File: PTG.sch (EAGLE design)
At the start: 96 parts, among them IC1 TPS62120, IC2 PIC32MK1024MCF064-I_PT, IC3 PCM1748, IC4 TPS561208, IC6 LT1762, IC7 LT1762, J1 STX31005NB, J2 RCJ-01X, J3 22-27-2021-02, SW1 ROCKER_SWITCH, SW2 ENCODER, SW3 MHPS2273N, SW4 MHPS2273N, SW5 MHPS2273N, SW6 MHPS2273N, X1 22-23-2041, Y1 EXTERNALCRYSTAL

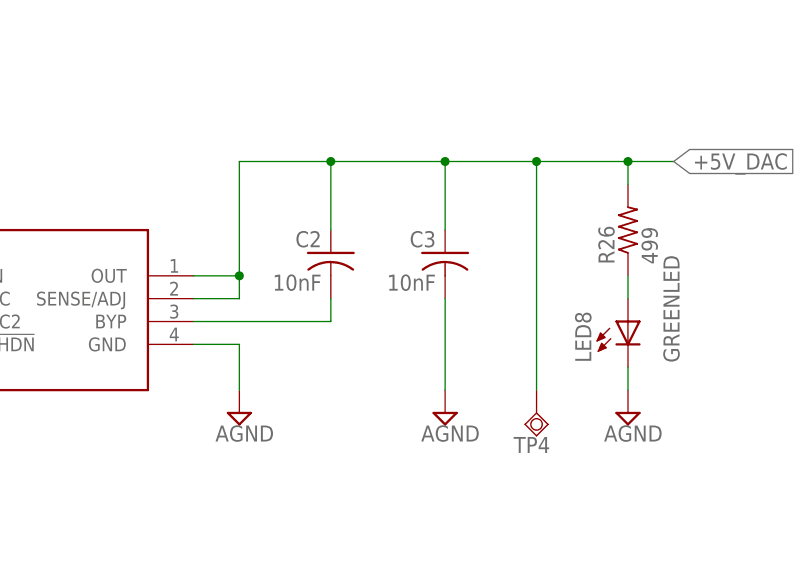
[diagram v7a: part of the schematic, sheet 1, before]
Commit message: fixed 10uF cap on IC6
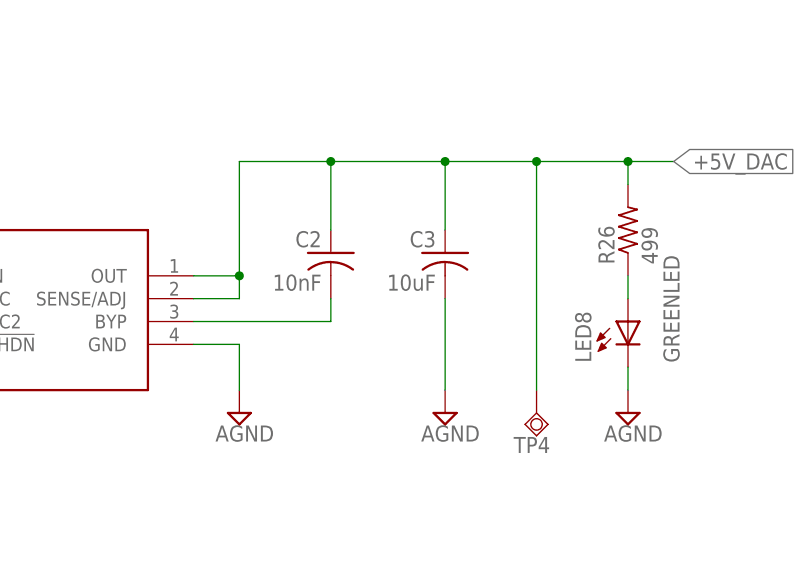
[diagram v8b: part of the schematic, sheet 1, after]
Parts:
- C3: value 10nF -> 10uF; device rcl:C-USC0603K -> rcl:C-USC0805K
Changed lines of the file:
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@@
 <grid distance="0.1" unitdist="inch" unit="inch" style="lines" multiple="1" display="no" altdistance="0.01" altunitdist="inch" altunit="inch"/>
 <layers>
-<layer number="1" name="Top" color="4" fill="1" visible="no" active="no"/>
-<layer number="2" name="Route2" color="3" fill="10" visible="no" active="no"/>
-<layer number="3" name="Route3" color="4" fill="3" visible="no" active="no"/>
-<layer number="4" name="Route4" color="1" fill="4" visible="no" active="no"/>
-<layer number="5" name="Route5" color="4" fill="4" visible="no" active="no"/>
-<layer number="6" name="Route6" color="1" fill="8" visible="no" active="no"/>
-<layer number="7" name="Route7" color="4" fill="8" visible="no" active="no"/>
-<layer number="8" name="Route8" color="1" fill="2" visible="no" active="no"/>
-<layer number="9" name="Route9" color="4" fill="2" visible="no" active="no"/>
-<layer number="10" name="Route10" color="1" fill="7" visible="no" active="no"/>
-<layer number="11" name="Route11" color="4" fill="7" visible="no" active="no"/>
-<layer number="12" name="Route12" color="1" fill="5" visible="no" active="no"/>
-<layer number="13" name="Route13" color="4" fill="5" visible="no" active="no"/>
-<layer number="14" name="Route14" color="1" fill="6" visible="no" active="no"/>
-<layer number="15" name="Route15" color="5" fill="4" visible="no" active="no"/>
-<layer number="16" name="Bottom" color="1" fill="1" visible="no" active="no"/>
-<layer number="17" name="Pads" color="2" fill="1" visible="no" active="no"/>
-<layer number="18" name="Vias" color="2" fill="1" visible="no" active="no"/>
-<layer number="19" name="Unrouted" color="60" fill="1" visible="no" active="no"/>
-<layer number="20" name="Dimension" color="15" fill="1" visible="no" active="no"/>
-<layer number="21" name="tPlace" color="7" fill="1" visible="no" active="no"/>
-<layer number="22" name="bPlace" color="7" fill="1" visible="no" active="no"/>
-<layer number="23" name="tOrigins" color="15" fill="1" visible="no" active="no"/>
-<layer number="24" name="bOrigins" color="15" fill="1" visible="no" active="no"/>
-<layer number="25" name="tNames" color="7" fill="1" visible="no" active="no"/>
-<layer number="26" name="bNames" color="7" fill="1" visible="no" active="no"/>
-<layer number="27" name="tValues" color="7" fill="1" visible="no" active="no"/>
-<layer number="28" name="bValues" color="7" fill="1" visible="no" active="no"/>
+<layer number="1" name="Top" color="4" fill="1" visible="yes" active="no"/>
+<layer number="2" name="Route2" color="3" fill="10" visible="yes" active="no"/>
+<layer number="3" name="Route3" color="4" fill="3" visible="yes" active="no"/>
+<layer number="4" name="Route4" color="1" fill="4" visible="yes" active="no"/>
+<layer number="5" name="Route5" color="4" fill="4" visible="yes" active="no"/>
+<layer number="6" name="Route6" color="1" fill="8" visible="yes" active="no"/>
+<layer number="7" name="Route7" color="4" fill="8" visible="yes" active="no"/>
+<layer number="8" name="Route8" color="1" fill="2" visible="yes" active="no"/>
+<layer number="9" name="Route9" color="4" fill="2" visible="yes" active="no"/>
+<layer number="10" name="Route10" color="1" fill="7" visible="yes" active="no"/>
+<layer number="11" name="Route11" color="4" fill="7" visible="yes" active="no"/>
+<layer number="12" name="Route12" color="1" fill="5" visible="yes" active="no"/>
+<layer number="13" name="Route13" color="4" fill="5" visible="yes" active="no"/>
+<layer number="14" name="Route14" color="1" fill="6" visible="yes" active="no"/>
+<layer number="15" name="Route15" color="5" fill="4" visible="yes" active="no"/>
+<layer number="16" name="Bottom" color="1" fill="1" visible="yes" active="no"/>
+<layer number="17" name="Pads" color="2" fill="1" visible="yes" active="no"/>
+<layer number="18" name="Vias" color="2" fill="1" visible="yes" active="no"/>
+<layer number="19" name="Unrouted" color="60" fill="1" visible="yes" active="no"/>
+<layer number="20" name="Dimension" color="15" fill="1" visible="yes" active="no"/>
+<layer number="21" name="tPlace" color="7" fill="1" visible="yes" active="no"/>
+<layer number="22" name="bPlace" color="7" fill="1" visible="yes" active="no"/>
+<layer number="23" name="tOrigins" color="15" fill="1" visible="yes" active="no"/>
+<layer number="24" name="bOrigins" color="15" fill="1" visible="yes" active="no"/>
+<layer number="25" name="tNames" color="7" fill="1" visible="yes" active="no"/>
+<layer number="26" name="bNames" color="7" fill="1" visible="yes" active="no"/>
+<layer number="27" name="tValues" color="7" fill="1" visible="yes" active="no"/>
+<layer number="28" name="bValues" color="7" fill="1" visible="yes" active="no"/>
 <layer number="29" name="tStop" color="7" fill="3" visible="no" active="no"/>
 <layer number="30" name="bStop" color="7" fill="6" visible="no" active="no"/>
@@
 <layer number="35" name="tGlue" color="7" fill="4" visible="no" active="no"/>
 <layer number="36" name="bGlue" color="7" fill="5" visible="no" active="no"/>
-<layer number="37" name="tTest" color="7" fill="1" visible="no" active="no"/>
-<layer number="38" name="bTest" color="7" fill="1" visible="no" active="no"/>
+<layer number="37" name="tTest" color="7" fill="1" visible="yes" active="no"/>
+<layer number="38" name="bTest" color="7" fill="1" visible="yes" active="no"/>
 <layer number="39" name="tKeepout" color="4" fill="11" visible="no" active="no"/>
 <layer number="40" name="bKeepout" color="1" fill="11" visible="no" active="no"/>
@@
 <layer number="44" name="Drills" color="7" fill="1" visible="no" active="no"/>
 <layer number="45" name="Holes" color="7" fill="1" visible="no" active="no"/>
-<layer number="46" name="Milling" color="3" fill="1" visible="no" active="no"/>
-<layer number="47" name="Measures" color="7" fill="1" visible="no" active="no"/>
-<layer number="48" name="Document" color="7" fill="1" visible="no" active="no"/>
-<layer number="49" name="Reference" color="7" fill="1" visible="no" active="no"/>
-<layer number="50" name="dxf" color="7" fill="1" visible="no" active="no"/>
-<layer number="51" name="tDocu" color="7" fill="1" visible="no" active="no"/>
-<layer number="52" name="bDocu" color="7" fill="1" visible="no" active="no"/>
-<layer number="53" name="tGND_GNDA" color="7" fill="9" visible="no" active="no"/>
-<layer number="54" name="bGND_GNDA" color="1" fill="9" visible="no" active="no"/>
-<layer number="56" name="wert" color="7" fill="1" visible="no" active="no"/>
+<layer number="46" name="Milling" color="3" fill="1" visible="yes" active="no"/>
+<layer number="47" name="Measures" color="7" fill="1" visible="yes" active="no"/>
+<layer number="48" name="Document" color="7" fill="1" visible="yes" active="no"/>
+<layer number="49" name="Reference" color="7" fill="1" visible="yes" active="no"/>
+<layer number="50" name="dxf" color="7" fill="1" visible="yes" active="no"/>
+<layer number="51" name="tDocu" color="7" fill="1" visible="yes" active="no"/>
+<layer number="52" name="bDocu" color="7" fill="1" visible="yes" active="no"/>
+<layer number="53" name="tGND_GNDA" color="7" fill="9" visible="yes" active="no"/>
+<layer number="54" name="bGND_GNDA" color="1" fill="9" visible="yes" active="no"/>
+<layer number="56" name="wert" color="7" fill="1" visible="yes" active="no"/>
 <layer number="90" name="Modules" color="5" fill="1" visible="yes" active="yes"/>
 <layer number="91" name="Nets" color="2" fill="1" visible="yes" active="yes"/>
@@
 <part name="+3V7" library="supply1" deviceset="+3V3" device=""/>
 <part name="J1" library="STX31005NB" deviceset="STX31005NB" device=""/>
-<part name="C3" library="rcl" deviceset="C-US" device="C0603K" value="10nF"/>
+<part name="C3" library="rcl" deviceset="C-US" device="C0805K" value="10uF"/>
 <part name="J3" library="con-molex" deviceset="22-?-02" device="27-2021"/>
 <part name="SUPPLY23" library="supply2" deviceset="GND" device=""/>
